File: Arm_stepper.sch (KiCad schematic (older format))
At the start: 132 parts, among them IC1 L6208D, IC2 L6208D, J1 12V_CONN, J10 ENCODER1, J11 ENCODER2, J2 M1_CONN, J3 M1_CONN, J4 Conn_01x06_Male, J5 I2C_CONN, J8 Conn_01x04_Female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

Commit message: relocating schematics
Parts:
- D4, D5, D6, D7, D8: footprint Diodes_SMD:D_1206 -> Diodes_SMD:D_SOD-123
- R47, R48: footprint (none) -> Resistors_SMD:R_1206_HandSoldering
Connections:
- net GNDS: no longer R33.1
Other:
- moved on the sheet: C26, C27, C34, C35, D10, D11, D12, D13, D14, D15, D16, D17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

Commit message: pcb design init
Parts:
- added HS1: Heatsink_Pad, SMD_Packages:1Pin, symbol Mechanical:Heatsink_Pad
- C13: renamed from 220nF1; value C -> 220nF1
- C15: renamed from 220nF2; value C -> 220nF1
- JP4, JP5: footprint Wire_Connections_Bridges:WireConnection_2.50mmDrill_LargePad -> Wire_Connections_Bridges:WireConnection_1.50mmDrill
- SW1: footprint Buttons_Switches_SMD:SW_SPST_PTS645 -> SMD_Packages:1Pin
- U2: footprint Package_TO_SOT_SMD:SOT-23-6 -> TO_SOT_Packages_SMD:SOT-23-6_Handsoldering
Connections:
- net GNDD: now also HS1.1
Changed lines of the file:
@@
 F 0 "SW1" H 2050 2785 50  0000 C CNN
 F 1 "SW_Push_Dual" H 2050 2694 50  0000 C CNN
-F 2 "Buttons_Switches_SMD:SW_SPST_PTS645" H 2050 2700 50  0001 C CNN
+F 2 "SMD_Packages:1Pin" H 2050 2700 50  0001 C CNN
 F 3 "" H 2050 2700 50  0001 C CNN
 	1    2050 2500
@@
 $EndComp
 $Comp
-L power:GNDS #PWR0103
-U 1 1 5C54E08D
-P 13000 3550
-F 0 "#PWR0103" H 13000 3300 50  0001 C CNN
-F 1 "GNDS" H 13005 3377 50  0000 C CNN
-F 2 "" H 13000 3550 50  0001 C CNN
-F 3 "" H 13000 3550 50  0001 C CNN
-	1    13000 3550
-	1    0    0    -1
-$EndComp
-$Comp
 L power:GNDS #PWR0104
 U 1 1 5C54E093
@@
 F 0 "U2" H 2650 10578 50  0000 C CNN
 F 1 "USBLC6-2SC6" H 2650 10487 50  0000 C CNN
-F 2 "Package_TO_SOT_SMD:SOT-23-6" H 1900 10300 50  0001 C CNN
+F 2 "TO_SOT_Packages_SMD:SOT-23-6_Handsoldering" H 1900 10300 50  0001 C CNN
 F 3 "http://www2.st.com/resource/en/datasheet/CD00050750.pdf" H 2850 10250 50  0001 C CNN
 	1    2650 9900
@@
 	9100 2050 9150 2050
 $Comp
-L Device:C 220nF2
+L Device:C C15
 U 1 1 5C8D1846
 P 8300 650
-F 0 "220nF2" V 8200 900 50  0000 C CNN
-F 1 "C" V 8300 850 50  0000 C CNN
+F 0 "C15" V 8200 900 50  0000 C CNN
+F 1 "220nF1" V 8300 850 50  0000 C CNN
 F 2 "Capacitors_SMD:C_1206_HandSoldering" H 8338 500 50  0001 C CNN
 F 3 "~" H 8300 650 50  0001 C CNN
@@
 	8900 5850 8950 5850
 $Comp
-L Device:C 220nF1
+L Device:C C13
 U 1 1 5C9FB45B
 P 8100 4450
-F 0 "220nF1" V 8000 4700 50  0000 C CNN
-F 1 "C" V 8100 4650 50  0000 C CNN
+F 0 "C13" V 8000 4700 50  0000 C CNN
+F 1 "220nF1" V 8100 4650 50  0000 C CNN
 F 2 "Capacitors_SMD:C_1206_HandSoldering" H 8138 4300 50  0001 C CNN
 F 3 "~" H 8100 4450 50  0001 C CNN
@@
 $EndComp
 $Comp
-L power:GNDD #PWR0109
-U 1 1 5C1F9193
-P 8300 5350
-F 0 "#PWR0109" H 8300 5100 50  0001 C CNN
-F 1 "GNDD" H 8304 5195 50  0000 C CNN
-F 2 "" H 8300 5350 50  0001 C CNN
-F 3 "" H 8300 5350 50  0001 C CNN
-	1    8300 5350
-	-1   0    0    1
-$EndComp
-$Comp
 L Jumper:SolderJumper_2_Bridged JP5
 U 1 1 5C226DB3
@@
 F 0 "JP5" V 9954 1318 50  0000 L CNN
 F 1 "SolderJumper_2_Bridged" V 10045 1318 50  0000 L CNN
-F 2 "Wire_Connections_Bridges:WireConnection_2.50mmDrill_LargePad" H 10000 1250 50  0001 C CNN
+F 2 "Wire_Connections_Bridges:WireConnection_1.50mmDrill" H 10000 1250 50  0001 C CNN
 F 3 "~" H 10000 1250 50  0001 C CNN
 	1    10000 1250
@@
 F 0 "JP4" V 9754 5118 50  0000 L CNN
 F 1 "SolderJumper_2_Bridged" V 9845 5118 50  0000 L CNN
-F 2 "Wire_Connections_Bridges:WireConnection_2.50mmDrill_LargePad" H 9800 5050 50  0001 C CNN
+F 2 "Wire_Connections_Bridges:WireConnection_1.50mmDrill" H 9800 5050 50  0001 C CNN
 F 3 "~" H 9800 5050 50  0001 C CNN
 	1    9800 5050
@@
 Wire Wire Line
 	10650 10250 10850 10250
+$Comp
+L power:GNDD #PWR0103
+U 1 1 5C3411B5
+P 8300 5400
+F 0 "#PWR0103" H 8300 5150 50  0001 C CNN
+F 1 "GNDD" H 8304 5245 50  0000 C CNN
+F 2 "" H 8300 5400 50  0001 C CNN
+F 3 "" H 8300 5400 50  0001 C CNN
+	1    8300 5400
+	0    -1   -1   0
+$EndComp
+$Comp
+L Mechanical:Heatsink_Pad HS1
+U 1 1 5C342A99
+P 8300 5250
+F 0 "HS1" H 8441 5291 50  0000 L CNN
+F 1 "Heatsink_Pad" H 8441 5200 50  0000 L CNN
+F 2 "SMD_Packages:1Pin" H 8312 5200 50  0001 C CNN
+F 3 "~" H 8312 5200 50  0001 C CNN
+	1    8300 5250
+	1    0    0    -1
+$EndComp
+Wire Wire Line
+	8300 5400 8300 5350
+Connection ~ 8300 5350
 $EndSCHEMATC

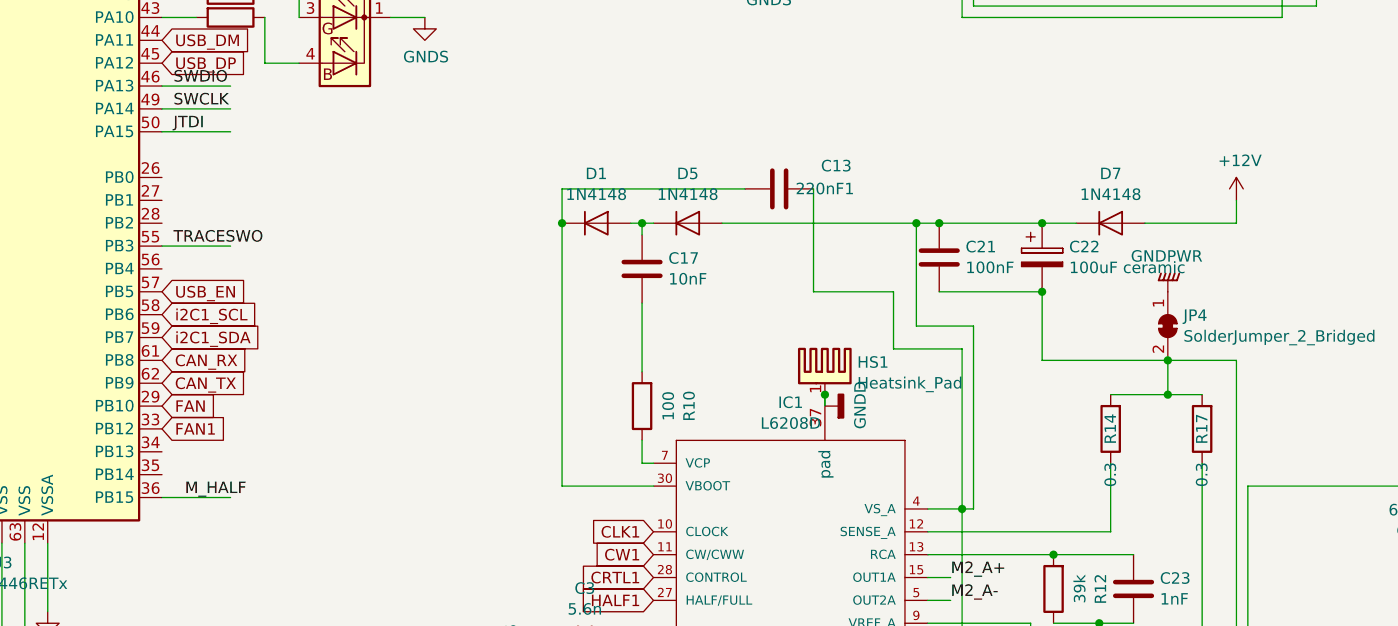
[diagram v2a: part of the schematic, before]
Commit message: mcu circuitry drawn
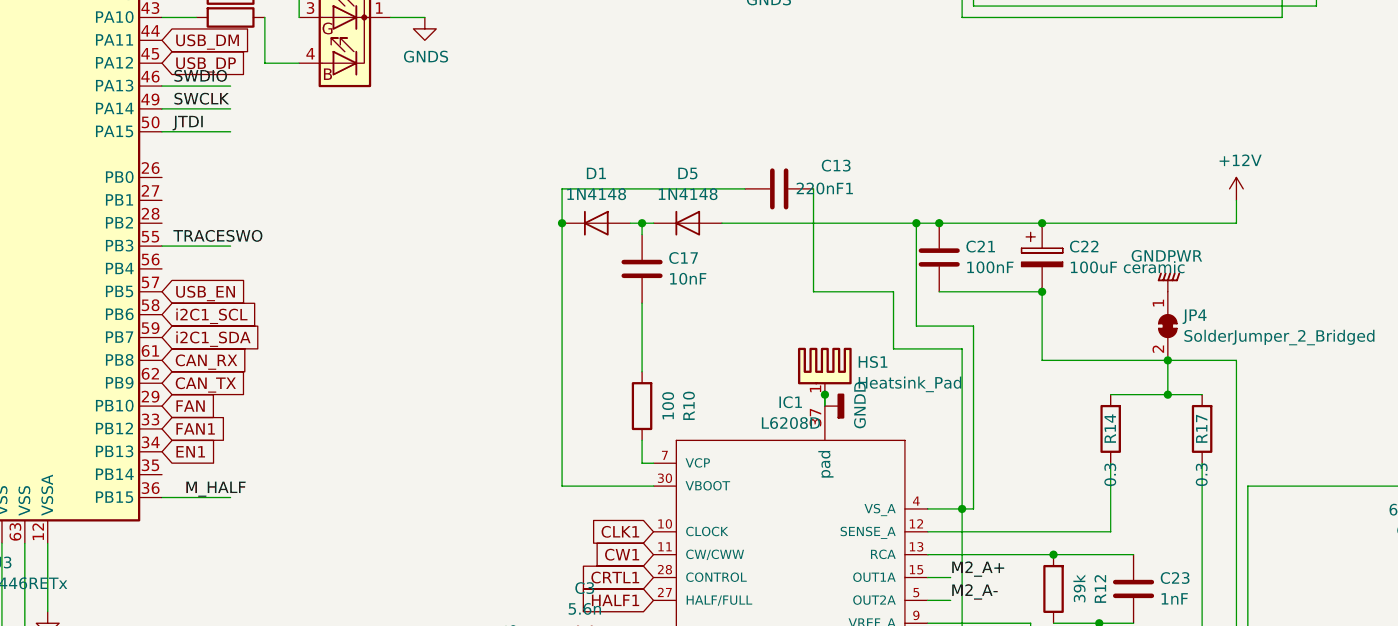
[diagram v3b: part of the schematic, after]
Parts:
- removed D7: 1N4148, Diodes_SMD:D_SOD-123, symbol Diode:1N4148
- SW1: footprint SMD_Packages:1Pin -> Buttons_Switches_THT:SW_TH_Tactile_Omron_B3F-10xx
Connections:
- net +12V: now also C13.1, C21.1, C22.1, D5.2 (A), IC1.33 (VS_B), IC1.4 (VS_A)
- net EN1: now also U3.34 (PB13)
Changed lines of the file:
@@
 F 0 "SW1" H 2050 2785 50  0000 C CNN
 F 1 "SW_Push_Dual" H 2050 2694 50  0000 C CNN
-F 2 "SMD_Packages:1Pin" H 2050 2700 50  0001 C CNN
+F 2 "Buttons_Switches_THT:SW_TH_Tactile_Omron_B3F-10xx" H 2050 2700 50  0001 C CNN
 F 3 "" H 2050 2700 50  0001 C CNN
 	1    2050 2500
@@
 Connection ~ 9300 6750
 $Comp
-L Diode:1N4148 D7
-U 1 1 5C9FB3BC
-P 9550 4600
-F 0 "D7" H 9550 4816 50  0000 C CNN
-F 1 "1N4148" H 9550 4725 50  0000 C CNN
-F 2 "Diodes_SMD:D_SOD-123" H 9550 4425 50  0001 C CNN
-F 3 "http://www.nxp.com/documents/data_sheet/1N4148_1N4448.pdf" H 9550 4600 50  0001 C CNN
-	1    9550 4600
-	1    0    0    -1
-$EndComp
-$Comp
 L Device:CP C22
 U 1 1 5C9FB3C2
@@
 	1    0    0    -1
 $EndComp
-Wire Wire Line
-	9250 4600 9400 4600
 $Comp
 L power:+12V #PWR039
@@
 $EndComp
 Wire Wire Line
-	9700 4600 10100 4600
-Wire Wire Line
 	10100 4600 10100 4500
 $Comp
@@
 	8300 5400 8300 5350
 Connection ~ 8300 5350
+Wire Wire Line
+	9250 4600 10100 4600
+Text GLabel 5400 5600 2    50   Input ~ 0
+EN1
 $EndSCHEMATC

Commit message: pcb design almost complete
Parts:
- R24: value 1K -> 27K
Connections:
- net +12V: now also M1.1 (+), M2.1 (+), R24.1
- net +3V3: no longer R24.1
- net +5V: no longer M1.1 (+), M2.1 (+)
- net FAN: now also U3.4 (PC15); no longer U3.29 (PB10)
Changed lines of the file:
@@
 	14850 8350 14850 8050
-$Comp
-L power:+5V #PWR087
-U 1 1 5C33E63A
-P 14850 7350
-F 0 "#PWR087" H 14850 7200 50  0001 C CNN
-F 1 "+5V" H 14865 7523 50  0000 C CNN
-F 2 "" H 14850 7350 50  0001 C CNN
-F 3 "" H 14850 7350 50  0001 C CNN
-	1    14850 7350
-	1    0    0    -1
-$EndComp
-Wire Wire Line
-	14850 7350 14850 7550
 $Comp
 L Device:R R31
@@
 Wire Wire Line
 	13350 8400 13350 8100
-$Comp
-L power:+5V #PWR075
-U 1 1 5C1FBCDB
-P 13350 7400
-F 0 "#PWR075" H 13350 7250 50  0001 C CNN
-F 1 "+5V" H 13365 7573 50  0000 C CNN
-F 2 "" H 13350 7400 50  0001 C CNN
-F 3 "" H 13350 7400 50  0001 C CNN
-	1    13350 7400
-	1    0    0    -1
-$EndComp
 Wire Wire Line
 	13350 7400 13350 7600
@@
 P 12150 8950
 F 0 "R24" H 12220 8996 50  0000 L CNN
-F 1 "1K" H 12220 8905 50  0000 L CNN
+F 1 "27K" H 12220 8905 50  0000 L CNN
 F 2 "Resistors_SMD:R_1206_HandSoldering" V 12080 8950 50  0001 C CNN
 F 3 "~" H 12150 8950 50  0001 C CNN
@@
 Text GLabel 4000 5700 0    50   Input ~ 0
 E1_2
-Text GLabel 5400 5400 2    50   Input ~ 0
+Text GLabel 4000 5800 0    50   Input ~ 0
 FAN
 Text GLabel 5400 5500 2    50   Input ~ 0
@@
 	9750 1850 9750 2150
 $Comp
-L power:+3.3V #PWR0112
-U 1 1 5D25828F
-P 12150 8800
-F 0 "#PWR0112" H 12150 8650 50  0001 C CNN
-F 1 "+3.3V" H 12165 8973 50  0000 C CNN
-F 2 "" H 12150 8800 50  0001 C CNN
-F 3 "" H 12150 8800 50  0001 C CNN
-	1    12150 8800
-	1    0    0    -1
-$EndComp
-$Comp
 L power:GNDPWR #PWR047
 U 1 1 5C2B9AD8
@@
 Text GLabel 5400 5600 2    50   Input ~ 0
 EN1
+$Comp
+L power:+12V #PWR0109
+U 1 1 5C5E36A7
+P 13350 7400
+F 0 "#PWR0109" H 13350 7250 50  0001 C CNN
+F 1 "+12V" H 13365 7573 50  0000 C CNN
+F 2 "" H 13350 7400 50  0001 C CNN
+F 3 "" H 13350 7400 50  0001 C CNN
+	1    13350 7400
+	1    0    0    -1
+$EndComp
+$Comp
+L power:+12V #PWR0110
+U 1 1 5C5E43B4
+P 14850 7550
+F 0 "#PWR0110" H 14850 7400 50  0001 C CNN
+F 1 "+12V" H 14865 7723 50  0000 C CNN
+F 2 "" H 14850 7550 50  0001 C CNN
+F 3 "" H 14850 7550 50  0001 C CNN
+	1    14850 7550
+	1    0    0    -1
+$EndComp
+$Comp
+L power:+12V #PWR?
+U 1 1 5C634527
+P 12150 8800
+F 0 "#PWR?" H 12150 8650 50  0001 C CNN
+F 1 "+12V" H 12165 8973 50  0000 C CNN
+F 2 "" H 12150 8800 50  0001 C CNN
+F 3 "" H 12150 8800 50  0001 C CNN
+	1    12150 8800
+	1    0    0    -1
+$EndComp
 $EndSCHEMATC

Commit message: copper completed
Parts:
- removed C6: 100nF, Capacitors_SMD:C_1206_HandSoldering, symbol Device:C
- removed JP1, JP2, JP3: SolderJumper_2_Bridged, Pin_Headers:Pin_Header_Angled_1x03_Pitch2.54mm, symbol Jumper:SolderJumper_2_Bridged
- removed M1: Fan, Pin_Headers:Pin_Header_Angled_1x02_Pitch2.54mm, symbol Motor:Fan
- removed Q1: 2N2219, TO_SOT_Packages_SMD:SOT-23, symbol Transistor_BJT:2N2219
- removed R27: 70k, Resistors_SMD:R_1206_HandSoldering, symbol Device:R
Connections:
- net GNDA is gone; now on net GNDS: U3.12 (VSSA)
- net +3V3: now also L1.2, U3.13 (VDDA)
- net NRST: now also R47.1, U3.7 (NRST)
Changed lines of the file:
@@
 Wire Wire Line
 	3550 3100 3700 3100
-$Comp
-L Device:C C6
-U 1 1 5BEB3213
-P 2600 7150
-F 0 "C6" H 2485 7104 50  0000 R CNN
-F 1 "100nF" H 2485 7195 50  0000 R CNN
-F 2 "Capacitors_SMD:C_1206_HandSoldering" H 2638 7000 50  0001 C CNN
-F 3 "~" H 2600 7150 50  0001 C CNN
-	1    2600 7150
-	-1   0    0    1
-$EndComp
 Text Notes 1000 6650 0    50   Italic 10
 Power Supply\nDecoupling
 $Comp
-L power:VDDA #PWR036
-U 1 1 5BEB425B
-P 5300 2400
-F 0 "#PWR036" H 5300 2250 50  0001 C CNN
-F 1 "VDDA" H 5317 2573 50  0000 C CNN
-F 2 "" H 5300 2400 50  0001 C CNN
-F 3 "" H 5300 2400 50  0001 C CNN
-	1    5300 2400
-	1    0    0    -1
-$EndComp
-$Comp
 L power:+3.3V #PWR01
 U 1 1 5BEC1743
@@
 Wire Wire Line
 	4600 1650 4600 2500
-$Comp
-L power:GNDA #PWR032
-U 1 1 5BED7686
-P 4900 6300
-F 0 "#PWR032" H 4900 6050 50  0001 C CNN
-F 1 "GNDA" H 4905 6127 50  0000 C CNN
-F 2 "" H 4900 6300 50  0001 C CNN
-F 3 "" H 4900 6300 50  0001 C CNN
-	1    4900 6300
-	1    0    0    -1
-$EndComp
 Wire Wire Line
 	4900 6000 4900 6300
 Text Notes 3100 7550 0    50   ~ 0
 Notes:\n1. 3V3 is used as VDD and VDDA for uC. Battery should be disconnected when debugging.
-$Comp
-L power:VDDA #PWR015
-U 1 1 5BEDDEFF
-P 2600 6900
-F 0 "#PWR015" H 2600 6750 50  0001 C CNN
-F 1 "VDDA" H 2617 7073 50  0000 C CNN
-F 2 "" H 2600 6900 50  0001 C CNN
-F 3 "" H 2600 6900 50  0001 C CNN
-	1    2600 6900
-	1    0    0    -1
-$EndComp
-Wire Wire Line
-	2600 6900 2600 7000
-$Comp
-L power:GNDA #PWR016
-U 1 1 5BEDEEB2
-P 2600 7400
-F 0 "#PWR016" H 2600 7150 50  0001 C CNN
-F 1 "GNDA" H 2605 7227 50  0000 C CNN
-F 2 "" H 2600 7400 50  0001 C CNN
-F 3 "" H 2600 7400 50  0001 C CNN
-	1    2600 7400
-	1    0    0    -1
-$EndComp
-Wire Wire Line
-	2600 7300 2600 7400
 Wire Notes Line
 	3000 6650 3000 7650
-Wire Notes Line
-	650  6650 3000 6650
-Wire Notes Line
-	650  7650 3000 7650
-$Comp
-L power:GNDA #PWR013
-U 1 1 5BEE0C53
-P 2200 6200
-F 0 "#PWR013" H 2200 5950 50  0001 C CNN
-F 1 "GNDA" H 2205 6027 50  0000 C CNN
-F 2 "" H 2200 6200 50  0001 C CNN
-F 3 "" H 2200 6200 50  0001 C CNN
-	1    2200 6200
-	1    0    0    -1
-$EndComp
 Wire Wire Line
 	4700 6000 4700 6900
@@
 Wire Wire Line
 	4800 6600 5050 6600
-Wire Wire Line
-	1750 6200 1750 6050
-Wire Wire Line
-	2200 6050 2200 6200
-$Comp
-L Jumper:SolderJumper_2_Bridged JP1
-U 1 1 5BF244FC
-P 2000 6050
-F 0 "JP1" H 2000 5917 50  0000 C CNN
-F 1 "SolderJumper_2_Bridged" H 2000 5916 50  0001 C CNN
-F 2 "Pin_Headers:Pin_Header_Angled_1x03_Pitch2.54mm" H 2000 6050 50  0001 C CNN
-F 3 "~" H 2000 6050 50  0001 C CNN
-	1    2000 6050
-	-1   0    0    1
-$EndComp
-Wire Wire Line
-	1750 6050 1850 6050
-Wire Wire Line
-	2200 6050 2150 6050
-Connection ~ 5000 2400
-Wire Wire Line
-	5000 2500 5000 2400
 $Comp
 L Connector:Conn_01x06_Male J4
@@
 Wire Wire Line
 	5300 1650 5300 1750
-$Comp
-L Jumper:SolderJumper_2_Bridged JP3
-U 1 1 5C01EA89
-P 5150 2400
-F 0 "JP3" H 5150 2267 50  0000 C CNN
-F 1 "SolderJumper_2_Bridged" V 5195 2468 50  0001 L CNN
-F 2 "Pin_Headers:Pin_Header_Angled_1x03_Pitch2.54mm" H 5150 2400 50  0001 C CNN
-F 3 "~" H 5150 2400 50  0001 C CNN
-	1    5150 2400
-	-1   0    0    1
-$EndComp
-Wire Wire Line
-	5000 1650 5000 1800
 Wire Wire Line
 	5300 2150 5300 2050
 Connection ~ 5000 2150
 Wire Wire Line
-	5000 2150 5000 2400
-Wire Wire Line
 	5000 2150 5300 2150
-$Comp
-L Jumper:SolderJumper_2_Bridged JP2
-U 1 1 5C022BD6
-P 5000 1950
-F 0 "JP2" V 5000 1862 50  0000 R CNN
-F 1 "SolderJumper_2_Bridged" V 5045 2018 50  0001 L CNN
-F 2 "Pin_Headers:Pin_Header_Angled_1x03_Pitch2.54mm" H 5000 1950 50  0001 C CNN
-F 3 "~" H 5000 1950 50  0001 C CNN
-	1    5000 1950
-	0    -1   -1   0
-$EndComp
-Wire Wire Line
-	5000 2100 5000 2150
 Wire Wire Line
 	5000 1650 5300 1650
@@
 $EndComp
 $Comp
-L power:GNDS #PWR011
-U 1 1 5BFFC7A0
-P 1750 6200
-F 0 "#PWR011" H 1750 5950 50  0001 C CNN
-F 1 "GNDS" H 1755 6027 50  0000 C CNN
-F 2 "" H 1750 6200 50  0001 C CNN
-F 3 "" H 1750 6200 50  0001 C CNN
-	1    1750 6200
-	1    0    0    -1
-$EndComp
-$Comp
 L power:GNDS #PWR02
 U 1 1 5BFFC832
@@
 $EndComp
 $Comp
-L Motor:Fan M1
-U 1 1 5C1FBCCE
-P 13350 7900
-F 0 "M1" H 13192 7904 50  0000 R CNN
-F 1 "Fan" H 13192 7995 50  0000 R CNN
-F 2 "Pin_Headers:Pin_Header_Angled_1x02_Pitch2.54mm" H 13350 7910 50  0001 C CNN
-F 3 "~" H 13350 7910 50  0001 C CNN
-	1    13350 7900
-	1    0    0    -1
-$EndComp
-$Comp
-L Transistor_BJT:2N2219 Q1
-U 1 1 5C1FBCD4
-P 13250 8600
-F 0 "Q1" H 13441 8554 50  0000 L CNN
-F 1 "2N2219" H 13441 8645 50  0000 L CNN
-F 2 "TO_SOT_Packages_SMD:SOT-23" H 13450 8525 50  0001 L CIN
-F 3 "http://www.onsemi.com/pub_link/Collateral/2N2219-D.PDF" H 13250 8600 50  0001 L CNN
-	1    13250 8600
-	1    0    0    -1
-$EndComp
-Wire Wire Line
-	13350 8400 13350 8100
-Wire Wire Line
-	13350 7400 13350 7600
-$Comp
-L Device:R R27
-U 1 1 5C1FBCE2
-P 12850 8600
-F 0 "R27" H 12920 8646 50  0000 L CNN
-F 1 "70k" H 12920 8555 50  0000 L CNN
-F 2 "Resistors_SMD:R_1206_HandSoldering" V 12780 8600 50  0001 C CNN
-F 3 "~" H 12850 8600 50  0001 C CNN
-	1    12850 8600
-	0    -1   -1   0
-$EndComp
-Wire Wire Line
-	13050 8600 13000 8600
-Text GLabel 12700 8600 0    50   Input ~ 0
-FAN1
-$Comp
 L Device:Thermistor_NTC TH1
 U 1 1 5C22299E
@@
 	9750 1850 9750 2150
 $Comp
-L power:GNDPWR #PWR047
-U 1 1 5C2B9AD8
-P 13350 8950
-F 0 "#PWR047" H 13350 8750 50  0001 C CNN
-F 1 "GNDPWR" H 13354 8796 50  0000 C CNN
-F 2 "" H 13350 8900 50  0001 C CNN
-F 3 "" H 13350 8900 50  0001 C CNN
-	1    13350 8950
-	1    0    0    -1
-$EndComp
-$Comp
 L power:GNDPWR #PWR048
 U 1 1 5C2DA61D
@@
 	1    0    0    -1
 $EndComp
-Wire Wire Line
-	13350 8950 13350 8800
 $Comp
 L power:GNDS #PWR020
@@
 EN1
 $Comp
-L power:+12V #PWR0109
-U 1 1 5C5E36A7
-P 13350 7400
-F 0 "#PWR0109" H 13350 7250 50  0001 C CNN
-F 1 "+12V" H 13365 7573 50  0000 C CNN
-F 2 "" H 13350 7400 50  0001 C CNN
-F 3 "" H 13350 7400 50  0001 C CNN
-	1    13350 7400
-	1    0    0    -1
-$EndComp
-$Comp
 L power:+12V #PWR0110
 U 1 1 5C5E43B4
@@
 $EndComp
 $Comp
-L power:+12V #PWR?
+L power:+12V #PWR0111
 U 1 1 5C634527
 P 12150 8800
-F 0 "#PWR?" H 12150 8650 50  0001 C CNN
+F 0 "#PWR0111" H 12150 8650 50  0001 C CNN
 F 1 "+12V" H 12165 8973 50  0000 C CNN
 F 2 "" H 12150 8800 50  0001 C CNN
@@
 	1    0    0    -1
 $EndComp
+Text Label 3800 2500 0    50   ~ 0
+NRST
+Wire Wire Line
+	5000 2150 5000 2500
+Wire Wire Line
+	5000 1650 5000 2150
+$Comp
+L power:GNDS #PWR0113
+U 1 1 5C3DDCE0
+P 4900 6300
+F 0 "#PWR0113" H 4900 6050 50  0001 C CNN
+F 1 "GNDS" V 4905 6172 50  0000 R CNN
+F 2 "" H 4900 6300 50  0001 C CNN
+F 3 "" H 4900 6300 50  0001 C CNN
+	1    4900 6300
+	1    0    0    -1
+$EndComp
